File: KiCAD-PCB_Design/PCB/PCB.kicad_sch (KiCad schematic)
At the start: 14 parts, among them SW1 SW_Push, SW2 SW_Push, SW3 SW_Push, SW4 SW_Push, SW5 SW_Push

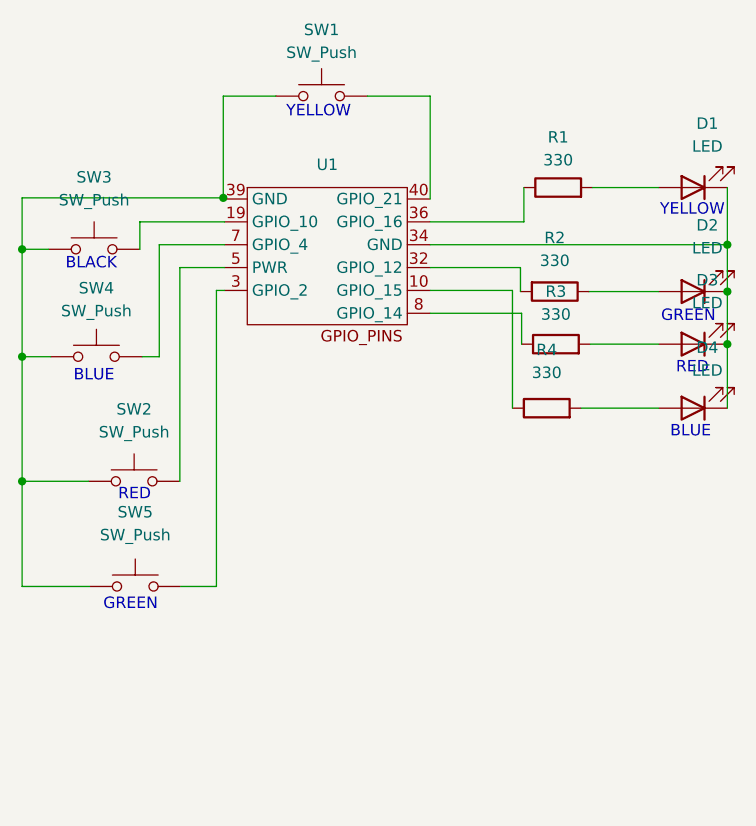
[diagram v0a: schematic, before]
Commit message: Latest PCB design, GPIO changes
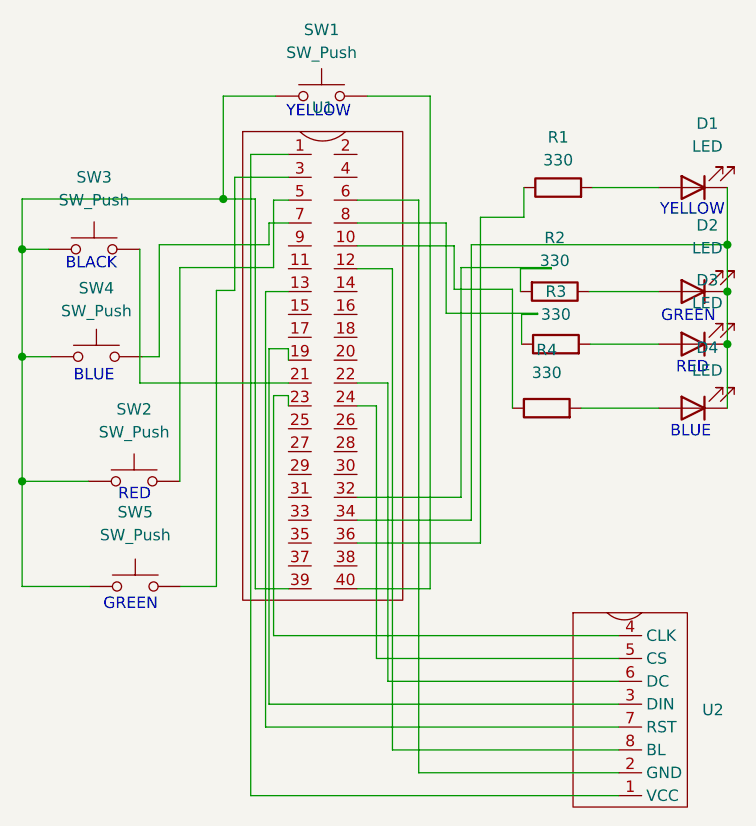
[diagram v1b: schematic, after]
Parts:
- removed U1: ~, Library:GPIO_PINS_TEST, symbol Symbols:GPIO_Pins
- added U1: ~, Library:Raspberry_Pi_Socketed_THT_FaceDown_MountingHoles, symbol Symbols:GPIO_HEADER_PINS
- added U2: ~, Library:LCD, symbol Symbols:LCD
- R1, R2, R3, R4: footprint Resistor_SMD:R_0201_0603Metric -> Resistor_THT:R_Axial_DIN0204_L3.6mm_D1.6mm_P1.90mm_Vertical
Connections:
- net at SW1.1, SW2.1, SW3.1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: now also U1.39
- net at SW2.2: now also U1.5
- net at SW1.2: now also U1.40
- net at R2.2: now also U1.32
- net at R1.1: now also U1.36
- net at D1.1 (K), D2.1 (K), D3.1 (K)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: now also U1.34
- net at SW5.2: now also U1.3
- net at R4.1: now also U1.10
- net at SW3.2: now also U1.21
- net at SW4.2: now also U1.7
- net at R3.1: now also U1.8
- new net: U1.1, U2.1 (VCC)
- new net: U1.12, U2.8 (BL)
- new net: U1.13, U2.7 (RST)
- new net: U1.19, U2.3 (DIN)
- new net: U1.22, U2.6 (DC)
- new net: U1.23, U2.4 (CLK)
- new net: U1.24, U2.5 (CS)
- new net: U1.6, U2.2 (GND)
